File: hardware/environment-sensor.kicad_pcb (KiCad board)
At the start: 2 copper layers, 109 x 84 mm, 112 parts, among them J1 J1B1211CCD, P1 USB_OTG, P2 ICSP, P3 JTAG, P4 NSL-19M51, P5 PPD42, P6 POWER, SW1 Reset, U1 ATMEGA32U4-AU, U2 W5500, U3 Bosch_BME280, U4 LT1761-5, U5 LT1761-3.3, X1 16MHz, X2 25MHz

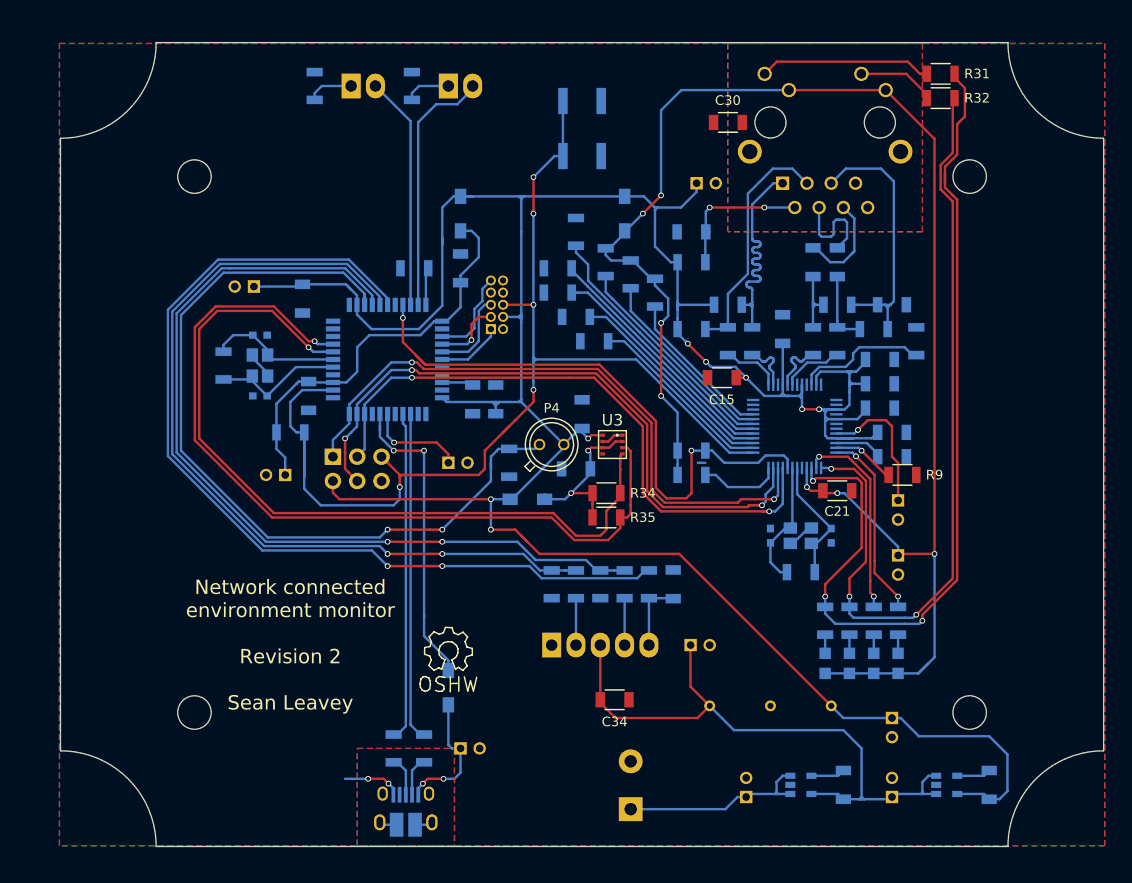
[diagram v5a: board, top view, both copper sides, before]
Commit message: Further update to change clock package and move some components around
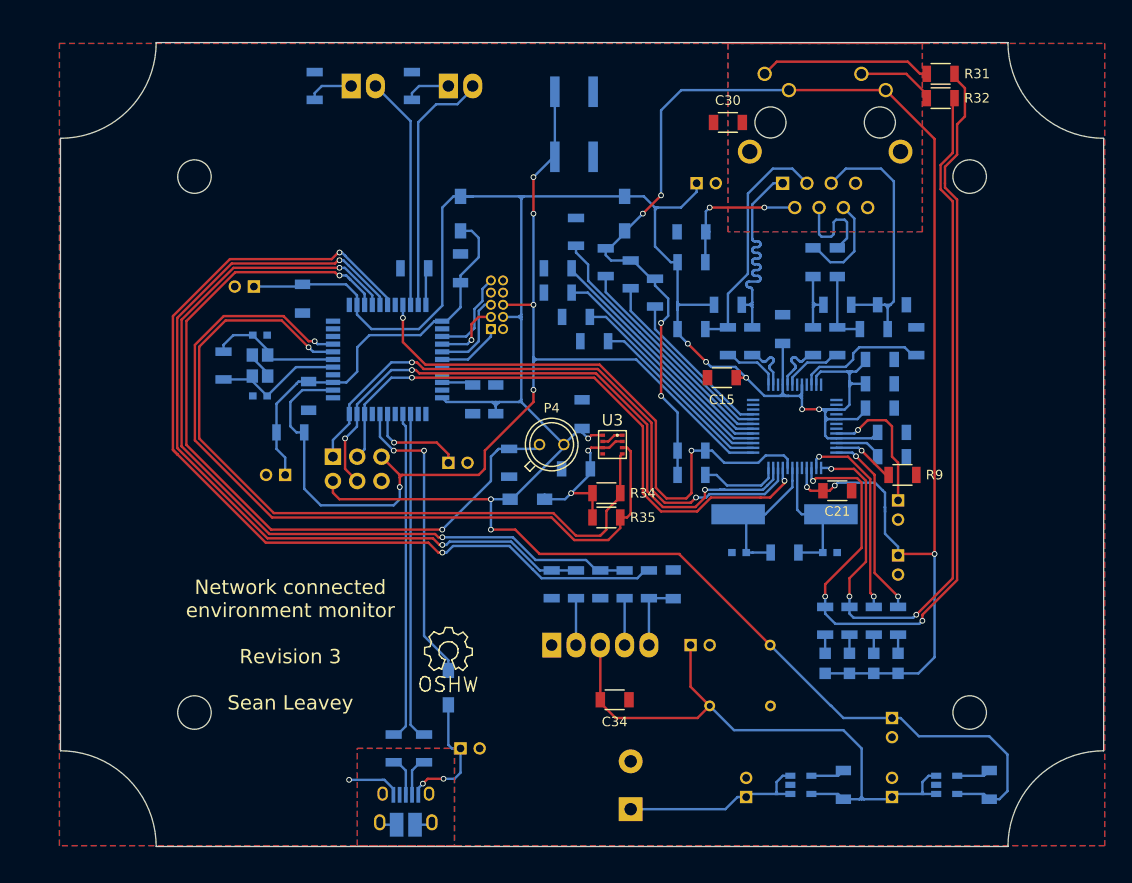
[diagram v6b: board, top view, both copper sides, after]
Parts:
- C24, C25: value 10p -> 32p
- SW1: footprint Buttons_Switches_SMD:SW_SPST_B3SL-1002P -> Buttons_Switches_SMD:SW_SPST_EVQP0
- X2: footprint Crystals:crystal_FA238-TSX3225 -> Crystals:Crystal_HC49-SD_SMD
- moved W2 9.00 mm to (176.5, 121.9)
- moved C25 3.72 mm to (173.2, 112.2), turned to 0 degrees
- moved X2 2.82 mm to (178.0, 108.2)
- moved R12 2.67 mm to (178.0, 112.2)
- moved C24 1.76 mm to (182.8, 112.2), turned to 180 degrees
- moved SW1 0.96 mm to (156.0, 67.5)
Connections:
- P1 pad 4: Net-(P1-Pad4) -> (no net)
- P3 pad 7: Net-(P3-Pad7) -> (no net)
- P3 pad 8: Net-(P3-Pad8) -> (no net)
- U1 pad 1: Net-(U1-Pad1) -> (no net)
- U1 pad 12: Net-(U1-Pad12) -> (no net)
- U1 pad 2: Net-(U1-Pad2) -> (no net)
- U1 pad 20: Net-(U1-Pad20) -> (no net)
- U1 pad 21: Net-(U1-Pad21) -> (no net)
- U1 pad 22: Net-(U1-Pad22) -> (no net)
- U1 pad 29: Net-(U1-Pad29) -> (no net)
- U1 pad 40: Net-(U1-Pad40) -> (no net)
- U1 pad 41: Net-(U1-Pad41) -> (no net)
- U1 pad 8: Net-(U1-Pad8) -> (no net)
- U2 pad 12: Net-(U2-Pad12) -> (no net)
- U2 pad 13: Net-(U2-Pad13) -> (no net)
- U2 pad 18: Net-(U2-Pad18) -> (no net)
- U2 pad 46: Net-(U2-Pad46) -> (no net)
- U2 pad 47: Net-(U2-Pad47) -> (no net)
- U2 pad 7: Net-(U2-Pad7) -> (no net)
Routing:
- net /Microcontroller/~RESET: track 119.6 -> 114.2 mm
- net /Microcontroller/3V3A: track 306.4 -> 301.9 mm
- net /Microcontroller/LDR_OUT: track 86.0 -> 82.1 mm
- net GND: track 14.6 -> 11.9 mm, vias 2 -> 1
- net /Network I/O/3V3D: track 164.7 -> 167.3 mm
- net Net-(C25-Pad2): track 13.7 -> 15.8 mm
- net /Microcontroller/I2C_SDA: track 88.0 -> 86.1 mm
- net /Microcontroller/I2C_SCLK: track 83.6 -> 81.7 mm
- net /Microcontroller/P_OUT_1: track 91.0 -> 89.2 mm
- net /Microcontroller/SS_PHY: track 62.8 -> 61.5 mm
- net /Microcontroller/SPI_SCLK: track 64.8 -> 63.6 mm
- net /Microcontroller/P_OUT_2: track 88.1 -> 87.0 mm
- net /Network I/O/ACTLED: track 94.8 -> 93.7 mm
- net /Microcontroller/SPI_MISO: track 66.1 -> 65.2 mm
- net Net-(P1-Pad6): track 3.73 -> 4.58 mm
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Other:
- board text added: "Network connected environment monitor Revision 3 Sean Leavey"
- board text added: "S/N:"
- board text removed: "Network connected environment monitor Revision 2 Sean Leavey"

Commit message: Revision to address clock issue
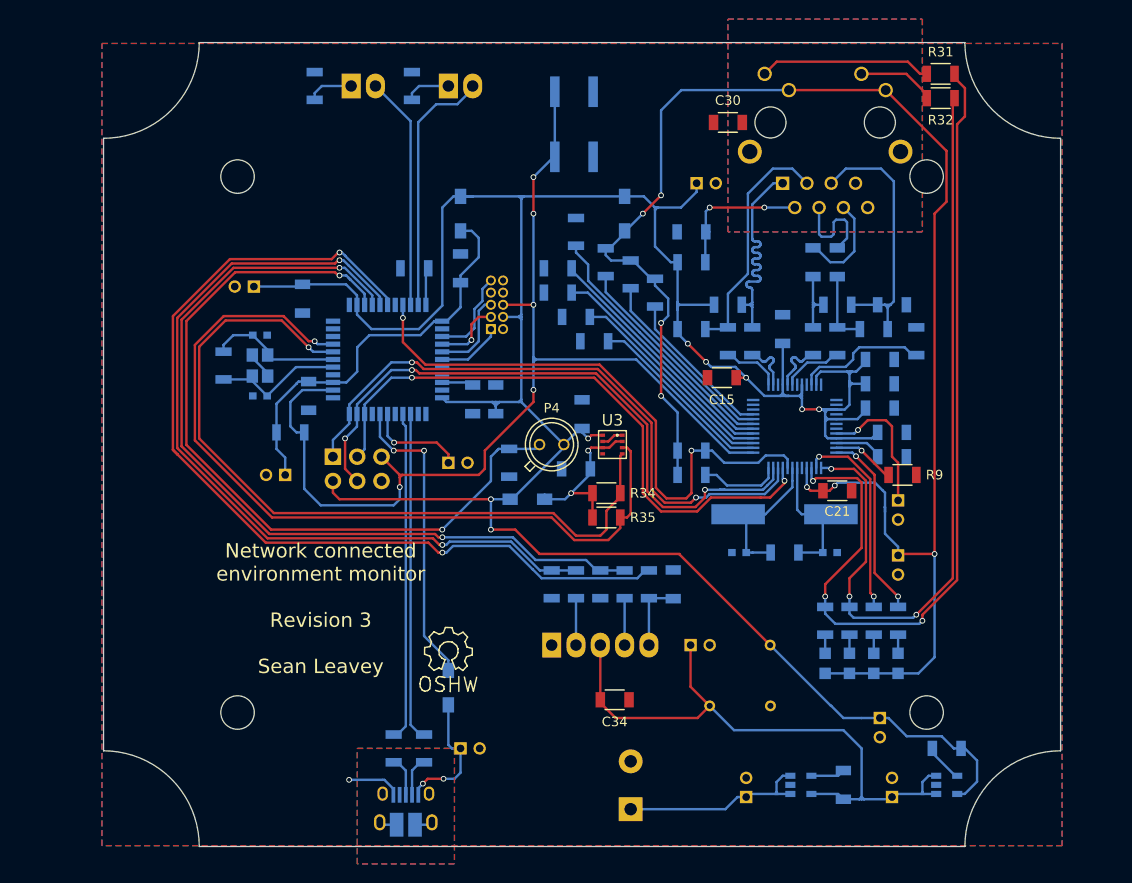
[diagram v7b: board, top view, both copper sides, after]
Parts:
- Ref**: footprint Board_Outlines:109mmx84mm_holes_b -> Board_Outlines:100mmx84mm_holes
- moved C38 5.85 mm to (194.9, 132.7), turned to 0 degrees
- moved C39 1.27 mm to (188.0, 129.5)
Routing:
- net /Microcontroller/3V3A: track 301.9 -> 294.2 mm
- net /Network I/O/ACTLED: track 93.7 -> 92.7 mm
- net /Network I/O/LINKLED: track 84.2 -> 83.2 mm
- net /Network I/O/3V3D: track 167.3 -> 168.4 mm
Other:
- board size 109 x 84 mm -> 100 x 84 mm
- board text added: "Reset"

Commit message: New revision to board
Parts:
- removed C15: 100n, Capacitors_SMD:C_1206
- removed D5: DUPLED, LEDs:LED_0805
- removed D6: ACTLED, LEDs:LED_0805
- removed R41, R42, R43: 330R, Resistors_SMD:R_1206
- removed REF**: Symbol_OSHW-Logo_SilkScreen, Symbols:Symbol_OSHW-Logo_SilkScreen
- removed the Ref** at (156.8, 101.0)
- added L5: Wurth WE-CBF, Choke_SMD:Choke_SMD_1206_Standard, F.Cu at (153.0, 94.6)
- added P7: JTAG, Pin_Headers:Pin_Header_Straight_2x05_Pitch1.27mm, F.Cu at (117.5, 86.4)
- added P8: DS18B20, Connectors_Molex:Molex_KK-6410-03_03x2.54mm_Straight, F.Cu at (144.8, 133.3)
- added P9: PPD42, Connectors_Molex:Molex_KK-6410-05_05x2.54mm_Straight, F.Cu at (128.3, 133.3)
- added REF***: OSHW-Logo_7.5x8mm_SilkScreen, Symbols:OSHW-Logo_7.5x8mm_SilkScreen, F.Cu at (155.6, 85.7)
- added Ref**: Val**, Board_Outlines:80mmx75mm_holes, F.Cu at (152.6, 101.6)
- C1, C10, C11, C12, C31, C32, C6, C7, C8, C9, L1, L2, L3, L4, R21, R36, R37, W1, W2, W3: moved to F.Cu
- C13, C33, C35, C37, C39: value 10u -> 100n; footprint Capacitors_ThroughHole:C_Radial_D5_L11_P2 -> Capacitors_SMD:C_1206; moved to F.Cu
- C14, C20: value 100n -> 10n; moved to F.Cu
- C16: value 100n -> 4u7; footprint Capacitors_SMD:C_1206 -> Capacitors_ThroughHole:C_Radial_D5_L11_P2; moved to F.Cu
- C17: value 100n -> 32p; footprint Capacitors_SMD:C_1206 -> Capacitors_SMD:C_0603; moved to F.Cu
- C18: value 10u -> 32p; footprint Capacitors_ThroughHole:C_Radial_D5_L11_P2 -> Capacitors_SMD:C_0603; moved to F.Cu
- C19: value 100n -> 22n; moved to F.Cu
- C2: value 12p -> 10n; footprint Capacitors_SMD:C_0603 -> Capacitors_SMD:C_1206; moved to F.Cu
- C21: value 100n -> 6.8n
- C22: value 10n -> 6.8n; moved to F.Cu
- C23: value 4u7 -> 1n/2kV; footprint Capacitors_ThroughHole:C_Radial_D5_L11_P2 -> Capacitors_SMD:C_1206; moved to F.Cu
- C24: value 32p -> 10u; footprint Capacitors_SMD:C_0603 -> Capacitors_ThroughHole:C_Radial_D5_L11_P2; moved to F.Cu
- C25: value 32p -> 12p; moved to F.Cu
- C26: value 22n -> 12p; footprint Capacitors_SMD:C_1206 -> Capacitors_SMD:C_0603; moved to F.Cu
- C27: value 10n -> 1u; footprint Capacitors_SMD:C_1206 -> Capacitors_ThroughHole:C_Radial_D5_L11_P2; moved to F.Cu
- C28: value 6.8n -> 100n; moved to F.Cu
- C29: value 6.8n -> 10u; footprint Capacitors_SMD:C_1206 -> Capacitors_ThroughHole:C_Radial_D5_L11_P2; moved to F.Cu
- C3: value 12p -> 10u; footprint Capacitors_SMD:C_0603 -> Capacitors_ThroughHole:C_Radial_D5_L11_P2; moved to F.Cu
- C30: value 1n/2kV -> 100n
- C34: value 100n -> 10u; footprint Capacitors_SMD:C_1206 -> Capacitors_ThroughHole:C_Radial_D5_L11_P2
- C36: value 10n -> 100n; moved to F.Cu
- C38: value 10n -> 10u; footprint Capacitors_SMD:C_1206 -> Capacitors_ThroughHole:C_Radial_D5_L11_P2; moved to F.Cu
- C4: value 1u -> 10n; footprint Capacitors_ThroughHole:C_Radial_D5_L11_P2 -> Capacitors_SMD:C_1206; moved to F.Cu
- C5: value 100n -> 10u; footprint Capacitors_SMD:C_1206 -> Capacitors_ThroughHole:C_Radial_D5_L11_P2; moved to F.Cu
- D1: value Status 1 -> LINKLED; footprint Connectors_Molex:Molex_KK-6410-02_02x2.54mm_Straight -> LEDs:LED_0805; moved to F.Cu
- D2: value Status 2 -> SPDLED; footprint Connectors_Molex:Molex_KK-6410-02_02x2.54mm_Straight -> LEDs:LED_0805; moved to F.Cu
- D3: value LINKLED -> DUPLED; moved to F.Cu
- D4: value SPDLED -> ACTLED; moved to F.Cu
- J1: footprint Cetus_RJ45:Cetus_J1B1211CCD -> Sockets_RJ45:Cetus_J1B1211CCD; moved to F.Cu
- P1: value USB_OTG -> POWER; footprint Connect:USB_Micro-B_10103594-0001LF -> Connectors_Molex:Molex_KK-6410-02_02x2.54mm_Straight; moved to F.Cu
- P2: value ICSP -> USB_OTG; footprint Pin_Headers:Pin_Header_Straight_2x03 -> Connect:USB_Micro-B_10103594-0001LF; moved to F.Cu
- P3: value JTAG -> ICSP; footprint Pin_Headers:Pin_Header_Straight_2x05_Pitch1.27mm -> Pin_Headers:Pin_Header_Straight_2x03; moved to F.Cu
- P4: value NSL-19M51 -> STATUS 1; footprint TO_SOT_Packages_THT:TO-18_2Pin -> Connectors_Molex:Molex_KK-6410-02_02x2.54mm_Straight
- P5: value PPD42 -> STATUS 2; footprint Connectors_Molex:Molex_KK-6410-05_05x2.54mm_Straight -> Connectors_Molex:Molex_KK-6410-02_02x2.54mm_Straight; moved to F.Cu
- P6: value POWER -> UART; footprint Terminal_Blocks:TerminalBlock_Pheonix_MKDS1.5-2pol -> Pin_Headers:Pin_Header_Straight_1x05; moved to F.Cu
- R1: value 10k -> 1M; moved to F.Cu
- R10, R11, R14: value 10k -> 49R9; moved to F.Cu
- R12: value 1M -> 10R; moved to F.Cu
- R13: value 12k4/1% -> 49R9; moved to F.Cu
- R15, R18, R19, R20: value 10k -> 330R; moved to F.Cu
- R16, R17: value 0R -> 330R; moved to F.Cu
- R2: value 22R -> 12k4/1%; moved to F.Cu
- R22, R23: value 10k -> 22R; moved to F.Cu
- R24: value 0R -> 1M; moved to F.Cu
- R25: value 0R -> 10k; moved to F.Cu
- R26, R27, R29: value 49R9/1% -> 10k; moved to F.Cu
- R28: value 10R/1% -> 10k; moved to F.Cu
- R3: value 22R -> 10k; moved to F.Cu
- R30: value 49R9/1% -> 180R; moved to F.Cu
- R31: value 330R -> 180R
- R32: value 330R -> 4k7
- R33, R38: value 10k -> 4k7; moved to F.Cu
- R34, R35: value 4k7 -> 10k
- R39: value 10k -> NSL-19M51; footprint Resistors_SMD:R_1206 -> LDRs_NSL:NSL_19M51
- R4: value 1M -> 10k; moved to F.Cu
- R40: value 330R -> 10k; moved to F.Cu
- R5, R8: value 10k -> 0R; moved to F.Cu
- R6: value 180R -> 0R; moved to F.Cu
- R7: value 180R -> 10k; moved to F.Cu
- R9: value 10k -> 0R
- SW1: value Reset -> RESET; footprint Buttons_Switches_SMD:SW_SPST_EVQP0 -> Buttons_Switches_SMD_FSM_JSM:SW_SPST_FSM_JSM; moved to F.Cu
- U1: value ATMEGA32U4-AU -> LT1761-5; footprint Housings_QFP:TQFP-44_10x10mm_Pitch0.8mm -> TO_SOT_Packages_SMD:SOT-23-5; moved to F.Cu
- U2: value W5500 -> LT1761-3.3; footprint Housings_QFP:LQFP-48_7x7mm_Pitch0.5mm -> TO_SOT_Packages_SMD:SOT-23-5; moved to F.Cu
- U3: value Bosch_BME280 -> W5500; footprint Bosch_Environment_Sensor:Bosch_BME280_LGA-8 -> Housings_QFP:LQFP-48_7x7mm_Pitch0.5mm
- U4: value LT1761-5 -> ATMEGA32U4-AU; footprint TO_SOT_Packages_SMD:SOT-23-5 -> Housings_QFP:TQFP-44_10x10mm_Pitch0.8mm; moved to F.Cu
- U5: value LT1761-3.3 -> Bosch_BME280; footprint TO_SOT_Packages_SMD:SOT-23-5 -> Sensors_LGA:Bosch_BME280_LGA-8
- X1: value 16MHz -> 25MHz; footprint Crystals:crystal_FA238-TSX3225 -> Crystals:Crystal_HC49-SD_SMD; moved to F.Cu
- X2: value 25MHz -> 16MHz; footprint Crystals:Crystal_HC49-SD_SMD -> Crystals:crystal_FA238-TSX3225; moved to F.Cu
- moved C2 77.0 mm to (188.6, 130.2), turned to 180 degrees
- moved C38 76.3 mm to (118.7, 135.9), turned to 90 degrees
- moved R31 74.9 mm to (170.8, 133.3), turned to 90 degrees
- moved U4 70.5 mm to (130.8, 85.7), turned to 90 degrees
- moved C24 68.3 mm to (130.2, 68.6), turned to 90 degrees
- moved R4 66.6 mm to (185.4, 101.6), turned to 180 degrees
- moved U1 66.4 mm to (188.6, 133.3)
- moved C3 65.9 mm to (182.9, 123.8), turned to 90 degrees
- moved P6 65.5 mm to (139.7, 77.5)
- moved C39 65.0 mm to (123.2, 134.4)
- moved C28 62.6 mm to (121.3, 88.3), turned to 180 degrees
- moved C6 61.6 mm to (186.7, 94.6), turned to 0 degrees
- moved SW1 61.4 mm to (121.3, 118.1), turned to 0 degrees
- moved C27 59.2 mm to (130.8, 95.9), turned to 270 degrees
- moved R7 58.4 mm to (185.4, 99.1), turned to 180 degrees
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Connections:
- C1 pad 1: Net-(C1-Pad1) -> /Power Supply/+6V
- C10 pad 1: GND -> /Microcontroller/3V3A
- C10 pad 2: /Microcontroller/3V3A -> GND
- C11 pad 1: /Microcontroller/3V3A -> /Network I/O/3V3D
- C12 pad 1: /Microcontroller/P_THRESH -> /Microcontroller/3V3A
- C13 pad 1: /Microcontroller/3V3A -> /Network I/O/3V3D
- C14 pad 1: /Microcontroller/3V3A -> GND
- C14 pad 2: GND -> Net-(C14-Pad2)
- C16 pad 1: /Microcontroller/3V3A -> Net-(C16-Pad1)
- C17 pad 1: /Microcontroller/3V3A -> GND
- C17 pad 2: GND -> Net-(C17-Pad2)
- C18 pad 1: /Network I/O/3V3D -> GND
- C18 pad 2: GND -> Net-(C18-Pad2)
- C19 pad 1: /Microcontroller/3V3A -> Net-(C19-Pad1)
- C2 pad 2: GND -> /Microcontroller/5VA
- C20 pad 1: /Microcontroller/3V3A -> Net-(C20-Pad1)
- C21 pad 1: /Network I/O/3V3D -> /Network I/O/RX2+
- C21 pad 2: GND -> /Network I/O/RX1+
- C22 pad 1: GND -> /Network I/O/RX2-
- C22 pad 2: Net-(C22-Pad2) -> /Network I/O/RX1-
- C23 pad 1: Net-(C23-Pad1) -> GND
- C23 pad 2: GND -> /Network I/O/CHGND
- C24 pad 1: GND -> Net-(C24-Pad1)
- C24 pad 2: Net-(C24-Pad2) -> GND
- C25 pad 1: GND -> Net-(C25-Pad1)
- C25 pad 2: Net-(C25-Pad2) -> GND
- C27 pad 1: Net-(C27-Pad1) -> /Microcontroller/3V3D
- C28 pad 1: /Network I/O/RX2+ -> Net-(C28-Pad1)
- C28 pad 2: /Network I/O/RX1+ -> GND
- C29 pad 1: /Network I/O/RX2- -> /Microcontroller/3V3D
- C29 pad 2: /Network I/O/RX1- -> GND
- C3 pad 1: Net-(C3-Pad1) -> /Microcontroller/5VA
- C30 pad 2: /Network I/O/CHGND -> /Microcontroller/3V3D
- C31 pad 1: /Microcontroller/3V3A -> GND
- C31 pad 2: GND -> /Microcontroller/3V3D
- C32 pad 1: /Sensors/3V3D -> GND
- C32 pad 2: GND -> /Microcontroller/3V3A
- C33 pad 1: /Power Supply/5VA -> GND
- C33 pad 2: GND -> /Microcontroller/3V3A
- C34 pad 1: GND -> /Microcontroller/3V3A
- C34 pad 2: /Power Supply/5VA -> GND
- C35 pad 1: /Power Supply/+6V -> /Microcontroller/DUST_2_THRESH
- C36 pad 1: Net-(C36-Pad1) -> /Microcontroller/3V3A
- C36 pad 2: /Power Supply/5VA -> GND
- C37 pad 1: /Power Supply/5VA -> /Sensors/3V3D
- C38 pad 1: Net-(C38-Pad1) -> /Microcontroller/5VA
- C38 pad 2: /Microcontroller/3V3A -> GND
- C39 pad 1: /Microcontroller/3V3A -> GND
- C39 pad 2: GND -> /Microcontroller/5VA
- C4 pad 2: GND -> /Microcontroller/3V3A
- C5 pad 1: Net-(C5-Pad1) -> /Microcontroller/3V3A
- C6 pad 1: /Microcontroller/3V3D -> /Microcontroller/3V3A
- C7 pad 1: GND -> /Microcontroller/3V3A
- C7 pad 2: /Microcontroller/3V3D -> GND
- C8 pad 1: GND -> /Microcontroller/3V3A
- C8 pad 2: /Microcontroller/3V3D -> GND
- C9 pad 1: GND -> /Microcontroller/3V3A
- C9 pad 2: /Microcontroller/3V3A -> GND
- D1 pad 2: Net-(D1-Pad2) -> /Network I/O/3V3D
- D2 pad 2: Net-(D2-Pad2) -> /Network I/O/3V3D
- J1 pad 2: Net-(C26-Pad1) -> Net-(C19-Pad1)
- J1 pad 5: Net-(C27-Pad1) -> Net-(C20-Pad1)
- L1 pad 1: /Microcontroller/3V3A -> /Network I/O/3V3D
- L1 pad 2: /Microcontroller/3V3D -> /Microcontroller/3V3A
- L2 pad 1: Net-(C1-Pad1) -> /Microcontroller/3V3A
- L2 pad 2: Net-(L2-Pad2) -> /Microcontroller/3V3D
- L3 pad 1: /Microcontroller/3V3A -> Net-(C24-Pad1)
- L3 pad 2: /Network I/O/3V3D -> Net-(L3-Pad2)
- L4 pad 1: /Microcontroller/3V3A -> Net-(L4-Pad1)
- L4 pad 2: /Sensors/3V3D -> /Microcontroller/5VA
- P1 pad 1: Net-(C1-Pad1) -> /Power Supply/+6V
- P1 pad 2: /Microcontroller/USBD- -> GND
- P2 pad 1: /Microcontroller/SPI_MISO -> Net-(C24-Pad1)
- P2 pad 2: /Microcontroller/3V3A -> /Microcontroller/USBD-
- P2 pad 3: /Microcontroller/SPI_SCLK -> /Microcontroller/USBD+
- P2 pad 4: /Microcontroller/SPI_MOSI -> (no net)
- P2 pad 5: /Microcontroller/~RESET -> GND
- P2 pad 6: GND -> Net-(P2-Pad6)
- P3 pad 1: Net-(P3-Pad1) -> /Microcontroller/SPI_MISO
- P3 pad 2: GND -> /Microcontroller/3V3A
- P3 pad 3: Net-(P3-Pad3) -> /Microcontroller/SPI_SCLK
- P3 pad 4: /Microcontroller/3V3A -> /Microcontroller/SPI_MOSI
- P3 pad 5: Net-(P3-Pad5) -> /Microcontroller/~RESET
- P3 pad 6: /Microcontroller/~RESET -> GND
- P4 pad 1: /Microcontroller/3V3A -> /Microcontroller/STATUS_1
- P4 pad 2: /Microcontroller/LDR_OUT -> Net-(P4-Pad2)
- P5 pad 1: GND -> /Microcontroller/STATUS_2
- P6 pad 1: /Power Supply/+6V -> /Microcontroller/3V3A
- P6 pad 2: GND -> Net-(P6-Pad2)
- R1 pad 1: /Microcontroller/3V3D -> Net-(C17-Pad2)
- R1 pad 2: /Microcontroller/~RESET -> Net-(C18-Pad2)
- R10 pad 1: /Network I/O/3V3D -> /Network I/O/TX1+
- R10 pad 2: /Microcontroller/SS_PHY -> /Microcontroller/3V3A
- R11 pad 1: /Network I/O/3V3D -> /Network I/O/TX1-
- R11 pad 2: Net-(R11-Pad2) -> /Microcontroller/3V3A
- R12 pad 1: Net-(C24-Pad2) -> Net-(C19-Pad1)
- R12 pad 2: Net-(C25-Pad2) -> /Microcontroller/3V3A
- R13 pad 1: GND -> Net-(C20-Pad1)
- R13 pad 2: Net-(R13-Pad2) -> /Network I/O/RX1+
- R14 pad 1: /Network I/O/3V3D -> Net-(C20-Pad1)
- R14 pad 2: Net-(R14-Pad2) -> /Network I/O/RX1-
- R15 pad 1: /Network I/O/3V3D -> Net-(J1-Pad9)
- R15 pad 2: Net-(R15-Pad2) -> /Network I/O/ACTLED
- R16 pad 1: /Network I/O/TX1+ -> Net-(J1-Pad11)
- R16 pad 2: /Network I/O/TX+ -> /Network I/O/LINKLED
- R17 pad 1: /Network I/O/RX1+ -> Net-(D1-Pad1)
- R17 pad 2: /Network I/O/RX+ -> /Network I/O/LINKLED
- R18 pad 1: GND -> Net-(D2-Pad1)
- R18 pad 2: Net-(R18-Pad2) -> /Network I/O/SPDLED
- R19 pad 1: GND -> Net-(D3-Pad1)
- R19 pad 2: Net-(R19-Pad2) -> /Network I/O/DUPLED
- R2 pad 1: /Microcontroller/USBD1+ -> GND
- R2 pad 2: /Microcontroller/USBD+ -> Net-(R2-Pad2)
- R20 pad 1: GND -> Net-(D4-Pad1)
- R20 pad 2: Net-(R20-Pad2) -> /Network I/O/ACTLED
- R21 pad 1: GND -> /Microcontroller/~RESET
- R21 pad 2: Net-(R21-Pad2) -> /Microcontroller/3V3D
- R22 pad 1: GND -> /Microcontroller/USBD+
- R22 pad 2: Net-(R22-Pad2) -> /Microcontroller/USBD1+
- R23 pad 1: /Network I/O/3V3D -> /Microcontroller/USBD-
- R23 pad 2: Net-(R23-Pad2) -> /Microcontroller/USBD1-
- R24 pad 1: /Network I/O/TX1- -> Net-(C26-Pad1)
- R24 pad 2: /Network I/O/TX- -> Net-(C25-Pad1)
- R25 pad 1: /Network I/O/RX1- -> Net-(R25-Pad1)
- R25 pad 2: /Network I/O/RX- -> GND
- R26 pad 1: /Network I/O/TX1+ -> /Microcontroller/DUST_2_THRESH
- R26 pad 2: /Microcontroller/3V3A -> Net-(R26-Pad2)
- R27 pad 1: /Network I/O/TX1- -> /Microcontroller/~PHY_INTERRUPT
- R27 pad 2: /Microcontroller/3V3A -> /Microcontroller/3V3D
- R28 pad 1: Net-(C26-Pad1) -> /Microcontroller/~PHY_RESET
- R28 pad 2: /Microcontroller/3V3A -> /Microcontroller/3V3D
- R29 pad 1: Net-(C27-Pad1) -> /Microcontroller/PHY_SS
- R29 pad 2: /Network I/O/RX1+ -> /Microcontroller/3V3D
- R3 pad 1: /Microcontroller/USBD1- -> /Microcontroller/3V3A
- R3 pad 2: /Microcontroller/USBD- -> Net-(R3-Pad2)
- R30 pad 1: Net-(C27-Pad1) -> GND
- R30 pad 2: /Network I/O/RX1- -> Net-(P4-Pad2)
- R31 pad 1: Net-(J1-Pad9) -> GND
- R31 pad 2: /Network I/O/ACTLED -> Net-(P5-Pad2)
- R32 pad 1: Net-(J1-Pad11) -> /Sensors/3V3D
- R32 pad 2: /Network I/O/LINKLED -> /Microcontroller/I2C_SCLK
- R33 pad 1: /Microcontroller/LDR_OUT -> /Sensors/3V3D
- R33 pad 2: GND -> /Microcontroller/I2C_SDA
- R34 pad 1: /Sensors/3V3D -> /Microcontroller/DUST_1
- R34 pad 2: /Microcontroller/I2C_SCLK -> Net-(P9-Pad4)
- R35 pad 1: /Sensors/3V3D -> GND
- R35 pad 2: /Microcontroller/I2C_SDA -> /Microcontroller/DUST_1
- R36 pad 1: /Microcontroller/P_OUT_1 -> /Microcontroller/DUST_2
- R36 pad 2: Net-(P5-Pad4) -> Net-(P9-Pad2)
- R37 pad 2: /Microcontroller/P_OUT_1 -> /Microcontroller/DUST_2
- R38 pad 1: /Microcontroller/P_OUT_2 -> /Microcontroller/DS18B20
- R38 pad 2: Net-(P5-Pad2) -> /Sensors/3V3D
- R39 pad 1: GND -> /Microcontroller/LDR
- R39 pad 2: /Microcontroller/P_OUT_2 -> /Microcontroller/3V3A
- R4 pad 1: Net-(C2-Pad1) -> /Microcontroller/3V3A
- R4 pad 2: Net-(C3-Pad1) -> Net-(R4-Pad2)
- R40 pad 1: Net-(D3-Pad1) -> /Microcontroller/LDR
- R40 pad 2: /Network I/O/LINKLED -> GND
- R5 pad 1: GND -> /Network I/O/TX1+
- R5 pad 2: Net-(R5-Pad2) -> /Network I/O/TX+
- R6 pad 1: GND -> /Network I/O/RX1+
- R6 pad 2: Net-(D1-Pad1) -> /Network I/O/RX+
- R7 pad 1: GND -> /Microcontroller/3V3A
- R7 pad 2: Net-(D2-Pad1) -> Net-(R7-Pad2)
- R8 pad 1: /Microcontroller/P_THRESH -> /Network I/O/TX1-
- R8 pad 2: Net-(R8-Pad2) -> /Network I/O/TX-
- R9 pad 1: Net-(R9-Pad1) -> /Network I/O/RX1-
- R9 pad 2: GND -> /Network I/O/RX-
- U1 pad 1: (no net) -> /Power Supply/+6V
- U1 pad 2: (no net) -> GND
- U1 pad 3: /Microcontroller/USBD1- -> /Power Supply/+6V
- U1 pad 4: /Microcontroller/USBD1+ -> Net-(C2-Pad1)
- U1 pad 5: GND -> /Microcontroller/5VA
- U2 pad 1: /Network I/O/TX- -> /Microcontroller/5VA
- U2 pad 2: /Network I/O/TX+ -> GND
- U2 pad 3: GND -> /Microcontroller/5VA
- U2 pad 4: /Microcontroller/3V3A -> Net-(C4-Pad1)
- U2 pad 5: /Network I/O/RX- -> /Microcontroller/3V3A
- U3 pad 1: GND -> /Network I/O/TX-
- U3 pad 2: /Sensors/3V3D -> /Network I/O/TX+
- U3 pad 3: /Microcontroller/I2C_SDA -> GND
- U3 pad 4: /Microcontroller/I2C_SCLK -> /Microcontroller/3V3A
- U3 pad 5: GND -> /Network I/O/RX-
- U3 pad 6: /Sensors/3V3D -> /Network I/O/RX+
- U3 pad 7: GND -> (no net)
- U4 pad 1: /Power Supply/+6V -> (no net)
- U4 pad 2: GND -> (no net)
- U4 pad 3: /Power Supply/+6V -> /Microcontroller/USBD1-
- U4 pad 4: Net-(C36-Pad1) -> /Microcontroller/USBD1+
- U4 pad 5: /Power Supply/5VA -> GND
- U5 pad 1: /Power Supply/5VA -> GND
- U5 pad 2: GND -> /Sensors/3V3D
- U5 pad 3: /Power Supply/5VA -> /Microcontroller/I2C_SDA
- U5 pad 4: Net-(C38-Pad1) -> /Microcontroller/I2C_SCLK
- U5 pad 5: /Microcontroller/3V3A -> GND
- W1 pad 1: /Power Supply/5VA -> /Microcontroller/5VA
- X1 pad 1: Net-(C2-Pad1) -> Net-(C18-Pad2)
- X1 pad 2: Net-(C3-Pad1) -> Net-(C17-Pad2)
- X2 pad 1: Net-(C25-Pad2) -> Net-(C25-Pad1)
- X2 pad 2: Net-(C24-Pad2) -> Net-(C26-Pad1)
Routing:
- net /Microcontroller/5VA: track 0.00 -> 162.5 mm, vias 0 -> 1
- net /Microcontroller/PHY_SS: track 0.00 -> 141.4 mm, vias 0 -> 2
- net /Microcontroller/STATUS_2: track 0.00 -> 122.2 mm, vias 0 -> 1
- net /Microcontroller/~PHY_INTERRUPT: track 0.00 -> 118.2 mm, vias 0 -> 2
- net /Microcontroller/STATUS_1: track 0.00 -> 116.1 mm, vias 0 -> 1
- net /Microcontroller/~PHY_RESET: track 0.00 -> 112.4 mm, vias 0 -> 2
- net Net-(R8-Pad2): track 98.7 -> 0.00 mm, vias 2 -> 0
- net /Microcontroller/DUST_2: track 0.00 -> 92.7 mm, vias 0 -> 2
- net /Microcontroller/P_OUT_1: track 89.2 -> 0.00 mm, vias 2 -> 0
- net /Microcontroller/DS18B20: track 0.00 -> 88.9 mm, vias 0 -> 2
- net Net-(R26-Pad2): track 0.00 -> 87.1 mm, vias 0 -> 2
- net /Microcontroller/P_OUT_2: track 87.0 -> 0.00 mm, vias 2 -> 0
- net /Microcontroller/DUST_1: track 0.00 -> 84.5 mm, vias 0 -> 2
- net /Microcontroller/LDR_OUT: track 82.1 -> 0.00 mm, vias 2 -> 0
- net /Power Supply/5VA: track 66.5 -> 0.00 mm
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- added copper zone on B.Cu, net Net-(P2-Pad6)
- added copper zone on F.Cu, net Net-(P2-Pad6)
- removed copper zone on B.Cu, net Net-(P1-Pad6)
- removed copper zone on F.Cu, net Net-(P1-Pad6)
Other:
- board size 100 x 84 mm -> 80 x 75 mm
- board text added: "+"
- board text added: "-"
- board text added: "3V3"
- board text added: "6-20V"
- board text added: "DS18B20"
- board text added: "Data"
- board text added: "Network connected environment monitor"
- board text added: "Power"
- board text added: "RXD"
- board text added: "S/N"
- board text added: "Sean Leavey"
- board text added: "TXD"
- board text added: "UART"
- board text removed: "3.3V"
- board text removed: "6V"
- board text removed: "Network connected environment monitor Revision 3 Sean Leavey"
- board text removed: "S/N:"
